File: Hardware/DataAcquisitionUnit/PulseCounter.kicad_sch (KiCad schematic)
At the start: 45 parts, among them J1 Conn_Coaxial, J2 Conn_Coaxial, J3 Conn_Coaxial, J4 Conn_Coaxial, U1 LM2901

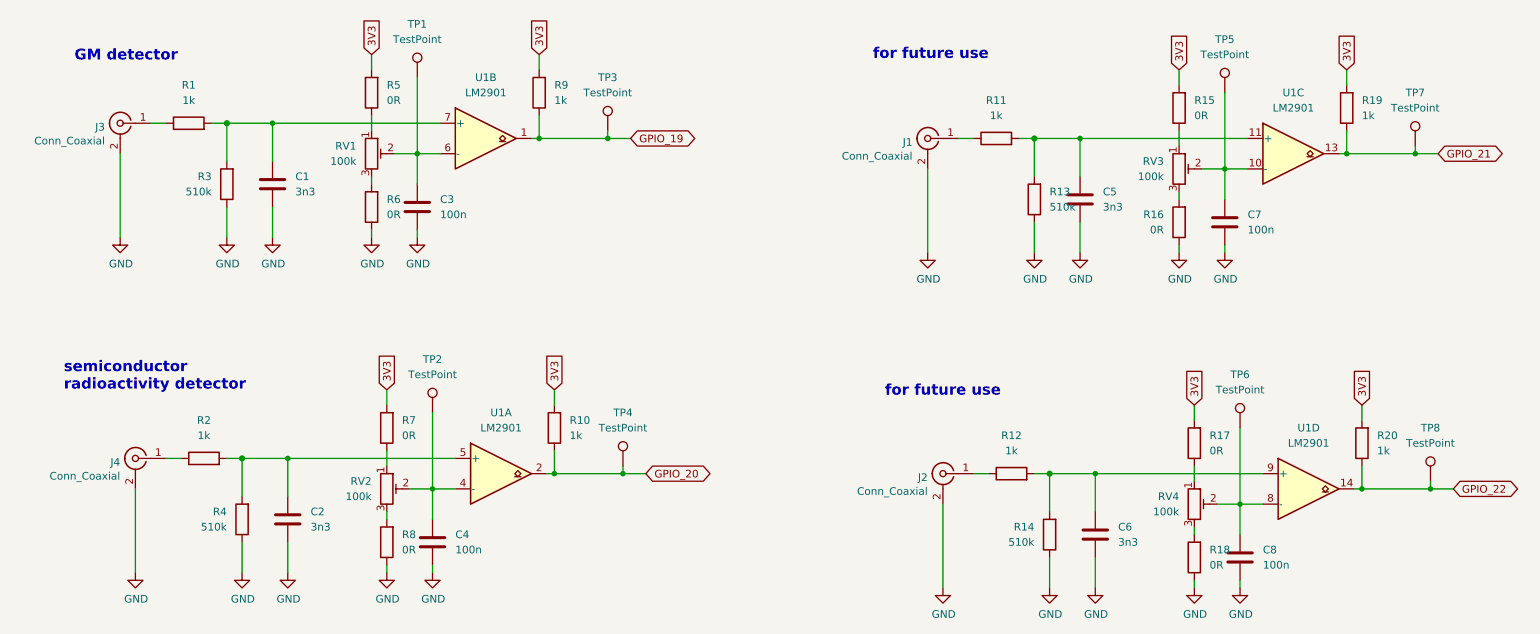
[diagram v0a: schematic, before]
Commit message: rework CI, make PCB smaller
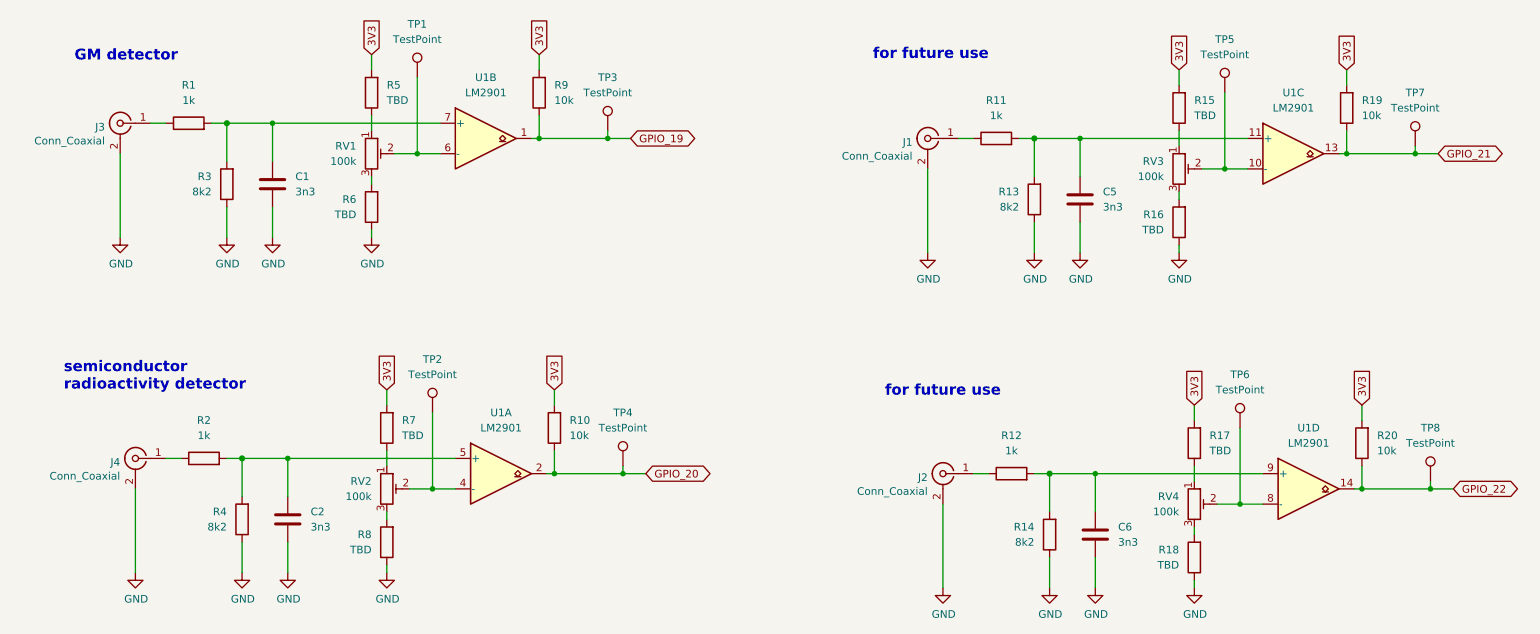
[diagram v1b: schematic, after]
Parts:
- removed C3, C4, C7, C8: 100n, Capacitor_SMD:C_0805_2012Metric, symbol Device:C
- R10, R19, R20, R9: value 1k -> 10k
- R13, R14, R3, R4: value 510k -> 8k2
- R15, R16, R17, R18, R5, R6, R7, R8: value 0R -> TBD
